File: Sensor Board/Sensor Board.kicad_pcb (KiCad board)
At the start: 2 copper layers, 40 x 40 mm, 34 parts, among them J1 Programming Header, J2 Irradience Sensor, J3 Micro_SD_Card, J4 CAN Bus Connector, U1 PIC18F26K83, U2 INA180, U4 MCP2562, U5 INA180, Y1 12MHz Crystal

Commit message: Fix review items
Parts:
- removed C8: 0.1uF, Capacitor_SMD:C_0805_2012Metric_Pad1.18x1.45mm_HandSolder
- removed J2: Irradience Sensor, Canhw:P16612-011CA
- added C10: 10nF, Capacitor_SMD:C_0805_2012Metric_Pad1.18x1.45mm_HandSolder, B.Cu at (117.8, 63.0)
- added C11: 1uF, Capacitor_SMD:C_0805_2012Metric_Pad1.18x1.45mm_HandSolder, B.Cu at (122.0, 72.2)
- added C12: 1.6pF, Capacitor_SMD:C_0805_2012Metric_Pad1.18x1.45mm_HandSolder, F.Cu at (137.5, 65.0)
- added C13: 1uF, Capacitor_SMD:C_0805_2012Metric_Pad1.18x1.45mm_HandSolder, F.Cu at (105.5, 60.0)
- added C9: 1uF, Capacitor_SMD:C_0805_2012Metric_Pad1.18x1.45mm_HandSolder, B.Cu at (104.9, 76.2)
- added D5: Irr Sense, Canhw:P16612-011CA, F.Cu at (135.5, 69.8)
- added R11: 1kR, Resistor_SMD:R_0805_2012Metric_Pad1.20x1.40mm_HandSolder, F.Cu at (110.8, 61.0)
- added R5: 47kR, Resistor_SMD:R_0805_2012Metric_Pad1.20x1.40mm_HandSolder, F.Cu at (105.5, 62.2)
- added TP1: 5v, TestPoint:TestPoint_Pad_1.5x1.5mm, F.Cu at (105.8, 66.5)
- added TP2: 3.3v, TestPoint:TestPoint_Pad_1.5x1.5mm, B.Cu at (117.5, 76.2)
- added TP3: TestPoint, TestPoint:TestPoint_Pad_1.5x1.5mm, F.Cu at (130.8, 57.8)
- added U3: SPX3819M5-L-3-3, Package_TO_SOT_SMD:SOT-23-5, B.Cu at (116.5, 68.8)
- C3, C4, C5, C6, C7, J1, J3, J4, R2, R3, R4, Y1: moved to B.Cu
- R1: value 180kR -> 5MR
- R10, R6, R7: value 330R -> 150R
- moved U5 113.3 mm to (107.2, 76.6), turned to -90 degrees
- moved F1 111.5 mm to (103.0, 76.5), turned to 90 degrees
- moved C7 109.3 mm to (118.2, 56.5), turned to -90 degrees
- moved R9 108.7 mm to (106.0, 69.4), turned to 180 degrees
- moved J1 94.2 mm to (111.0, 59.4), turned to -90 degrees
- moved U2 87.7 mm to (133.9, 62.9), turned to -90 degrees
- moved D4 86.4 mm to (116.5, 55.2), turned to 90 degrees
- moved C6 85.8 mm to (108.2, 76.2), turned to 90 degrees
- moved C5 82.7 mm to (111.2, 76.2), turned to 90 degrees
- moved R1 78.7 mm to (137.5, 61.0), turned to 90 degrees
- moved Y1 75.0 mm to (127.5, 86.2), turned to 90 degrees
- moved C4 74.9 mm to (121.3, 56.7), turned to -90 degrees
- moved C3 71.8 mm to (122.0, 70.0), turned to 180 degrees
- moved R8 70.6 mm to (106.0, 72.2)
- moved C1 70.5 mm to (125.5, 84.0), turned to -90 degrees
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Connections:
- net CURR_SENSE renamed /CURR_SENSE
- C1 pad 2: Net-(C1-Pad2) -> GND
- C2 pad 2: Net-(C1-Pad2) -> GND
- C3 pad 2: +5V -> +3.3V
- J3 pad 4: +5V -> +3.3V
- J3 pad 9: unconnected-(J3-SHIELD-Pad9) -> GND
- J4 pad 2: CANL -> /CANH
- J4 pad 3: CANH -> /CANL
- R1 pad 1: +5V -> Net-(D5-A)
- R1 pad 2: Net-(U2-IN-) -> /IRR_SENSE
- R2 pad 1: +5V -> +3.3V
- R3 pad 1: +5V -> +3.3V
- R4 pad 1: +5V -> +3.3V
- U1 pad 25: IRR_SENSE -> /IRR_SENSE
- U2 pad 1: IRR_SENSE -> /IRR_SENSE
- U2 pad 3: +5V -> Net-(U2-IN+)
- U2 pad 4: Net-(U2-IN-) -> Net-(D5-A)
- U4 pad 1: /CANRX -> /CANTX
- U4 pad 4: /CANTX -> /CANRX
- U4 pad 6: CANL -> /CANL
- U4 pad 7: CANH -> /CANH
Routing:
- net GND: track 0.00 -> 120.8 mm, vias 0 -> 6
- net +5V: track 0.00 -> 61.2 mm, vias 0 -> 1
- net /IRR_SENSE: track 0.00 -> 50.7 mm
- net Net-(U2-IN+): track 0.00 -> 39.4 mm, vias 0 -> 2
- net +3.3V: track 0.00 -> 36.8 mm
- net /CANH: track 0.00 -> 32.4 mm
- net /CANL: track 0.00 -> 28.5 mm
- net Net-(D5-A): track 0.00 -> 20.0 mm
- net Net-(J4-Pin_5): track 0.00 -> 18.4 mm
- net /PIC_MICRO_SD_CS: track 0.00 -> 17.0 mm, vias 0 -> 1
- net /OSC1: track 0.00 -> 16.6 mm
- net /PIC_MICRO_SD_SDI: track 0.00 -> 14.9 mm, vias 0 -> 1
- net Net-(J3-DAT2): track 0.00 -> 12.6 mm
- net /PIC_MICRO_SD_SCK: track 0.00 -> 12.4 mm, vias 0 -> 1
- net /OSC2: track 0.00 -> 12.2 mm
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- added copper zone on B.Cu, net GND

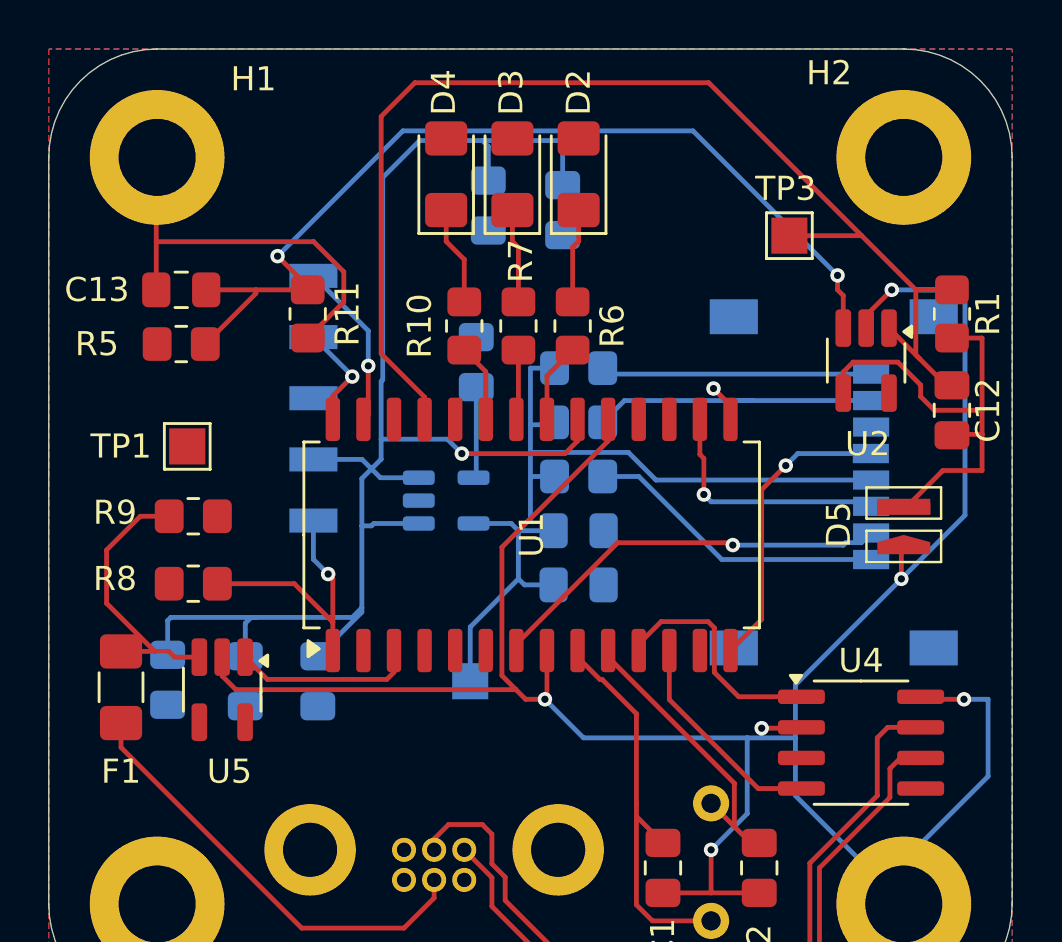
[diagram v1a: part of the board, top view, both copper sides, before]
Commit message: Switch op amp
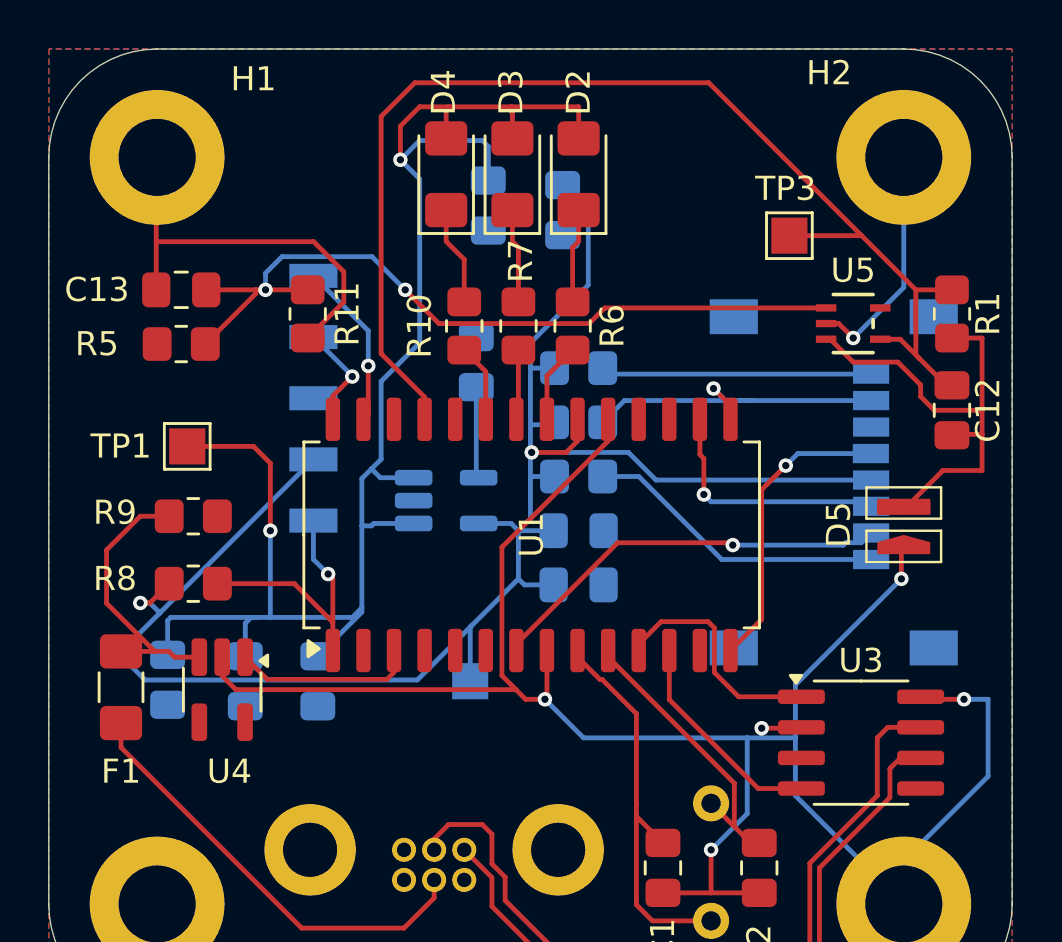
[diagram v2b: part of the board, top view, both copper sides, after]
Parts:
- removed the U2 at (133.9, 62.9)
- added U5: OPA323IDCKR, Canhw:SC70-5_DCK_TEX, F.Cu at (133.4, 61.4)
- C12: value 1.6pF -> 2.5pF
- R1: value 5MR -> 3MR
- R10: value 150R -> 220R
- R5: value 47kR -> 31kR
- R6, R7: value 150R -> 120R
- U2: renamed from U3; footprint Package_TO_SOT_SMD:SOT-23-5 -> Package_TO_SOT_SMD:SOT-23-5_HandSoldering
- renumbered U4 to U3, U5 to U4
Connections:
- C4 pad 1: +5V -> +3.3V
- J1 pad 4: +5V -> +3.3V
- R8 pad 1: +5V -> +3.3V
- U1 pad 20: +5V -> +3.3V
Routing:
- net +3.3V: track 36.8 -> 78.8 mm, vias 0 -> 2
- net GND: track 120.8 -> 112.4 mm
- net +5V: track 61.2 -> 67.9 mm, vias 1 -> 2
- net Net-(U5-IN+): track 39.4 -> 33.2 mm

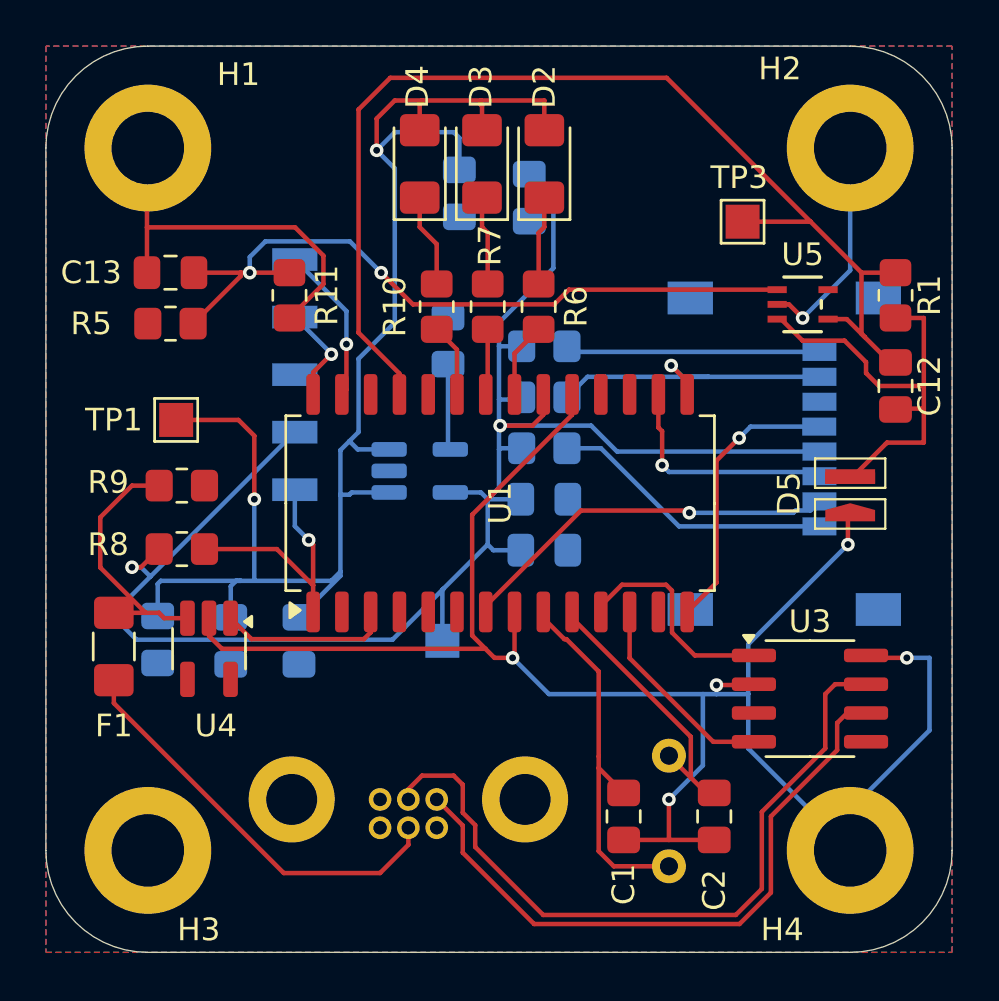
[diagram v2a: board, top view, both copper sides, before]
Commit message: Fix the traces and comments from Pranav
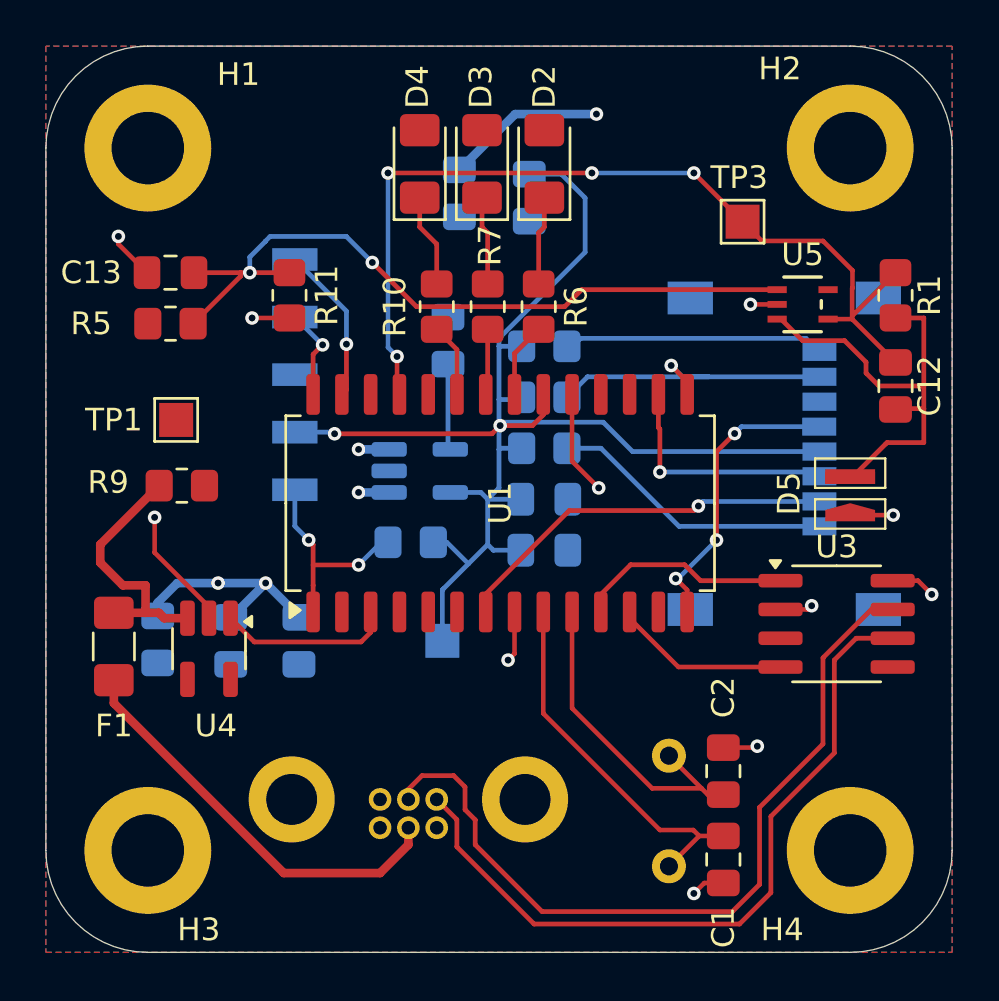
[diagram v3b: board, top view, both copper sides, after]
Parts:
- R8: moved to B.Cu
- moved R8 10.1 mm to (116.1, 71.9), turned to 180 degrees
- moved C1 4.79 mm to (129.9, 85.9)
- moved U3 3.50 mm to (134.9, 75.5)
- moved C2 2.04 mm to (129.9, 82.0), turned to 90 degrees
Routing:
- net GND: track 112.4 -> 25.7 mm, vias 6 -> 11
- net +5V: track 67.9 -> 20.0 mm, vias 2 -> 5
- net +3.3V: track 78.8 -> 63.0 mm
- net /IRR_SENSE: track 50.8 -> 40.9 mm, vias 0 -> 4
- net /CANL: track 28.5 -> 32.7 mm
- net /CANH: track 32.4 -> 35.5 mm
- net /OSC2: track 12.2 -> 14.5 mm
- net /~{MCLR}: track 11.2 -> 9.45 mm, vias 1 -> 2
- net /CANRX: track 9.05 -> 7.83 mm
- net /PIC_MICRO_SD_SCK: track 12.4 -> 13.1 mm, vias 1 -> 3
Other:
- board text added: "MCLR"

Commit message: Cooked another layout-Pranav
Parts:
- C12, C13, R1, R10, R11, R5, R6, R7, U4, U5: moved to B.Cu
- C3, J1, J4, R2, R3, R4, TP2: moved to F.Cu
- Y1: value 12MHz Crystal -> 12MHz Crystal; moved to F.Cu
- moved H3 133.9 mm to (230.6, 130.5)
- moved H1 125.8 mm to (204.7, 130.6)
- moved H4 96.5 mm to (230.6, 101.7)
- moved H2 85.6 mm to (206.4, 102.5)
- moved J1 54.3 mm to (161.9, 78.3)
- moved C13 52.2 mm to (149.8, 87.7), turned to 180 degrees
- moved C9 49.9 mm to (153.6, 87.1)
- moved C7 48.8 mm to (142.9, 98.7), turned to 0 degrees
- moved R5 48.2 mm to (148.4, 84.3), turned to 90 degrees
- moved D4 46.4 mm to (157.5, 77.0), turned to 180 degrees
- moved C10 45.2 mm to (157.7, 84.3), turned to 180 degrees
- moved F1 44.9 mm to (143.8, 95.3), turned to -90 degrees
- moved U2 44.9 mm to (157.4, 87.0)
- moved R11 44.1 mm to (145.8, 87.7), turned to 180 degrees
- moved R9 43.9 mm to (141.6, 95.1), turned to -90 degrees
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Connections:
- R10 pad 2: Net-(U1-RB2) -> Net-(U1-RC6)
- R5 pad 2: +5V -> +3.3V
- R6 pad 2: Net-(U1-RB0) -> Net-(U1-RC4)
- R7 pad 2: Net-(U1-RB1) -> Net-(U1-RC5)
- U1 pad 11: /CANTX -> unconnected-(U1-RC0-Pad11)
- U1 pad 12: /CANRX -> unconnected-(U1-RC1-Pad12)
- U1 pad 14: /PIC_MICRO_SD_SCK -> unconnected-(U1-RC3-Pad14)
- U1 pad 15: /PIC_MICRO_SD_SDI -> Net-(U1-RC4)
- U1 pad 16: /PIC_MICRO_SD_SDO -> Net-(U1-RC5)
- U1 pad 17: unconnected-(U1-RC6-Pad17) -> Net-(U1-RC6)
- U1 pad 18: unconnected-(U1-RC7-Pad18) -> /IRR_SENSE
- U1 pad 21: Net-(U1-RB0) -> /PIC_MICRO_SD_CS
- U1 pad 22: Net-(U1-RB1) -> /PIC_MICRO_SD_SDO
- U1 pad 23: Net-(U1-RB2) -> /PIC_MICRO_SD_SCK
- U1 pad 24: unconnected-(U1-RB3-Pad24) -> /PIC_MICRO_SD_SDI
- U1 pad 25: /IRR_SENSE -> /CANRX
- U1 pad 26: unconnected-(U1-RB5-Pad26) -> /CANTX
- U1 pad 3: /CURR_SENSE -> unconnected-(U1-RA1-Pad3)
- U1 pad 4: unconnected-(U1-RA2-Pad4) -> /CURR_SENSE
- U1 pad 7: /PIC_MICRO_SD_CS -> unconnected-(U1-RA5-Pad7)
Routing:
- net +5V: track 20.0 -> 88.6 mm, vias 5 -> 9
- net +3.3V: track 63.0 -> 13.9 mm, vias 2 -> 6
- net Net-(U5-IN+): track 33.4 -> 6.71 mm, vias 2 -> 0
- net /ICSPDAT: track 4.10 -> 23.2 mm, vias 1 -> 0
- net /~{MCLR}: track 9.45 -> 25.7 mm
- net /ICSPCLK: track 6.98 -> 22.9 mm, vias 1 -> 0
- net /CANH: track 35.5 -> 21.8 mm, vias 0 -> 3
- net /CANL: track 32.7 -> 19.1 mm, vias 0 -> 2
- net Net-(J3-DAT2): track 12.6 -> 2.32 mm, vias 0 -> 1
- net Net-(U1-RC4): track 0.00 -> 9.56 mm, vias 0 -> 1
- net Net-(D5-A): track 20.1 -> 10.8 mm, vias 0 -> 1
- net Net-(J3-DAT1): track 11.5 -> 2.36 mm, vias 0 -> 1
- net GND: track 25.7 -> 33.2 mm, vias 11 -> 63
- net /PIC_MICRO_SD_CS: track 17.2 -> 9.98 mm
- net Net-(U1-RC5): track 0.00 -> 6.29 mm, vias 0 -> 1
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- added copper zone on B.Cu, net +3.3V
- added copper zone on F.Cu, net GND
- removed copper zone on F.Cu, net +5V
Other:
- board outline removed
- board text removed: "MCLR"
